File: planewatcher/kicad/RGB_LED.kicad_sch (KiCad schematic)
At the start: 4 parts

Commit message: Add persistent PCBWay BOM fields to KiCad schematic
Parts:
- D1: MPN (none) -> APHF1608SEEQBDZGKC; Manufacturer (none) -> Kingbright; Package (none) -> SOD-123F
- R3: MPN (none) -> RC0402FR-071KL; Manufacturer (none) -> Yageo; Package (none) -> 0402
- R4, R5: MPN (none) -> RC0402FR-07665RL; Manufacturer (none) -> Yageo; Package (none) -> 0402
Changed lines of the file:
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@@
+			)
+		)
+		(property "Package" "SOD-123F"
+			(at 111.76 83.82 0)
+			(hide yes)
+			(show_name no)
+			(do_not_autoplace no)
+			(effects
+				(font
+					(size 1.27 1.27)
+				)
+			)
+		)
+		(property "MPN" "APHF1608SEEQBDZGKC"
+			(at 111.76 83.82 0)
+			(hide yes)
+			(show_name no)
+			(do_not_autoplace no)
+			(effects
+				(font
+					(size 1.27 1.27)
+				)
+			)
+		)
+		(property "Manufacturer" "Kingbright"
+			(at 111.76 83.82 0)
+			(hide yes)
+			(show_name no)
+			(do_not_autoplace no)
+			(effects
+				(font
+					(size 1.27 1.27)
+				)
 			)
 		)
@@
 			)
 		)
+		(property "Package" "0402"
+			(at 133.35 87.63 0)
+			(hide yes)
+			(show_name no)
+			(do_not_autoplace no)
+			(effects
+				(font
+					(size 1.27 1.27)
+				)
+			)
+		)
+		(property "MPN" "RC0402FR-07665RL"
+			(at 133.35 87.63 0)
+			(hide yes)
+			(show_name no)
+			(do_not_autoplace no)
+			(effects
+				(font
+					(size 1.27 1.27)
+				)
+			)
+		)
+		(property "Manufacturer" "Yageo"
+			(at 133.35 87.63 0)
+			(hide yes)
+			(show_name no)
+			(do_not_autoplace no)
+			(effects
+				(font
+					(size 1.27 1.27)
+				)
+			)
+		)
 		(property "Suggested Part" "Yageo RC0402FR-07665RL"
 			(at 133.35 87.63 0)
@@
 			)
 		)
+		(property "Package" "0402"
+			(at 144.78 82.55 0)
+			(hide yes)
+			(show_name no)
+			(do_not_autoplace no)
+			(effects
+				(font
+					(size 1.27 1.27)
+				)
+			)
+		)
+		(property "MPN" "RC0402FR-07665RL"
+			(at 144.78 82.55 0)
+			(hide yes)
+			(show_name no)
+			(do_not_autoplace no)
+			(effects
+				(font
+					(size 1.27 1.27)
+				)
+			)
+		)
+		(property "Manufacturer" "Yageo"
+			(at 144.78 82.55 0)
+			(hide yes)
+			(show_name no)
+			(do_not_autoplace no)
+			(effects
+				(font
+					(size 1.27 1.27)
+				)
+			)
+		)
 		(property "Suggested Part" "Yageo RC0402FR-07665RL"
 			(at 144.78 82.55 0)
@@
 			(at 123.19 92.71 0)
 			(hide yes)
+			(show_name no)
+			(do_not_autoplace no)
+			(effects
+				(font
+					(size 1.27 1.27)
+				)
+			)
+		)
+		(property "Package" "0402"
+			(at 123.19 92.71 0)
+			(hide yes)
+			(show_name no)
+			(do_not_autoplace no)
+			(effects
+				(font
+					(size 1.27 1.27)
+				)
+			)
+		)
+		(property "MPN" "RC0402FR-071KL"
+			(at 123.19 92.71 0)
+			(hide yes)
+			(show_name no)
+			(do_not_autoplace no)
+			(effects
+				(font
+					(size 1.27 1.27)
+				)
+			)
+		)
+		(property "Manufacturer" "Yageo"
+			(at 123.19 92.71 0)
+			(hide yes)

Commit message: move power supply and add GPS module
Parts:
- renumbered D1 to LED4
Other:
- title: (none) -> Plane Watcher
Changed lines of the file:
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@@
 	(paper "A4")
 	(title_block
-		(date "2026-05-16")
-		(rev "prototype 1.1")
+		(title "Plane Watcher")
+		(date "2026-05-18")
+		(rev "prototype 1.2")
 		(company "plane.watch")
 	)
@@
 		(in_pos_files yes)
 		(dnp no)
-		(property "Reference" "D1"
+		(property "Reference" "LED4"
 			(at 111.76 71.12 0)
 			(show_name no)
@@
 			(project "planewatcher"
 				(path "/7a4a4324-e8b8-4d06-b75a-28095d4e9f10/52b32cc6-d826-42d3-aa96-9038a73a9bfc"
-					(reference "D5")
+					(reference "LED1")
 					(unit 1)
 				)
 				(path "/7a4a4324-e8b8-4d06-b75a-28095d4e9f10/59545c86-c058-4e69-82ad-a37ead5abf92"
-					(reference "D1")
+					(reference "LED4")
 					(unit 1)
 				)
 				(path "/7a4a4324-e8b8-4d06-b75a-28095d4e9f10/7739f02d-62c0-4bca-89eb-2791de83397a"
-					(reference "D4")
+					(reference "LED3")
 					(unit 1)
 				)
 				(path "/7a4a4324-e8b8-4d06-b75a-28095d4e9f10/8d837c64-f9ae-4d10-9c5f-d514a90db394"
-					(reference "D6")
+					(reference "LED5")
 					(unit 1)
 				)
 				(path "/7a4a4324-e8b8-4d06-b75a-28095d4e9f10/d4f7e37f-a721-4dfe-b190-52f36600c34c"
-					(reference "D7")
-					(unit 1)
-				)
+					(reference "LED2")
+					(unit 1)
+				)

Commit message: review & consolidate all capacitors
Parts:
- LED4: Suggested Part Kingbright APHF1608SEEQBDZGKC -> (none)
- R3: Suggested Part Yageo RC0402FR-071KL -> (none)
- R4, R5: Suggested Part Yageo RC0402FR-07665RL -> (none)
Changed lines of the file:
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@@
 			)
 		)
-		(property "Suggested Part" "Kingbright APHF1608SEEQBDZGKC"
+		(property "Purpose" "Common-anode RGB status indicator driven by FPGA GPIO pins."
 			(at 111.76 83.82 0)
 			(hide yes)
@@
 			)
 		)
-		(property "Purpose" "Common-anode RGB status indicator driven by FPGA GPIO pins."
+		(property "Mount_Type" ""
 			(at 111.76 83.82 0)
 			(hide yes)
@@
 			)
 		)
-		(property "Suggested Part" "Yageo RC0402FR-07665RL"
-			(at 133.35 87.63 0)
-			(hide yes)
-			(show_name no)
-			(do_not_autoplace no)
-			(effects
-				(font
-					(size 1.27 1.27)
-				)
-			)
-		)
 		(property "Purpose" "Current-limit resistor for an FPGA-driven RGB status LED channel."
+			(at 133.35 87.63 0)
+			(hide yes)
+			(show_name no)
+			(do_not_autoplace no)
+			(effects
+				(font
+					(size 1.27 1.27)
+				)
+			)
+		)
+		(property "Mount_Type" ""
 			(at 133.35 87.63 0)
 			(hide yes)
@@
 			)
 		)
-		(property "Suggested Part" "Yageo RC0402FR-07665RL"
-			(at 144.78 82.55 0)
-			(hide yes)
-			(show_name no)
-			(do_not_autoplace no)
-			(effects
-				(font
-					(size 1.27 1.27)
-				)
-			)
-		)
 		(property "Purpose" "Current-limit resistor for an FPGA-driven RGB status LED channel."
+			(at 144.78 82.55 0)
+			(hide yes)
+			(show_name no)
+			(do_not_autoplace no)
+			(effects
+				(font
+					(size 1.27 1.27)
+				)
+			)
+		)
+		(property "Mount_Type" ""
 			(at 144.78 82.55 0)
 			(hide yes)
@@
 			)
 		)
-		(property "Suggested Part" "Yageo RC0402FR-071KL"
-			(at 123.19 92.71 0)
-			(hide yes)
-			(show_name no)
-			(do_not_autoplace no)
-			(effects
-				(font
-					(size 1.27 1.27)
-				)
-			)
-		)
 		(property "Purpose" "Current-limit resistor for an FPGA-driven RGB status LED channel."
 			(at 123.19 92.71 0)
 			(hide yes)
+			(show_name no)
+			(do_not_autoplace no)
+			(effects
+				(font
+					(size 1.27 1.27)
+				)
+			)
+		)
+		(property "Mount_Type" ""
+			(at 123.19 92.71 0)
+			(hide yes)

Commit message: review & consolidate all resistors
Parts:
- R3, R4, R5: Manufacturer Yageo -> YAGEO; Package 0402 -> 0402 (1005 Metric)
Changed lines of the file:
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@@
 			)
 		)
-		(property "Datasheet" "https://www.yageogroup.com/component-documentation/download/specsheet/RC0402FR-07665RL"
-			(at 133.35 87.63 0)
-			(hide yes)
-			(show_name no)
-			(do_not_autoplace no)
-			(effects
-				(font
-					(size 1.27 1.27)
-				)
-			)
-		)
-		(property "Description" "665Ω, ±1%, thick film, 100ppm/°C, 0402 chip resistor"
-			(at 133.35 87.63 0)
-			(hide yes)
-			(show_name no)
-			(do_not_autoplace no)
-			(effects
-				(font
-					(size 1.27 1.27)
-				)
-			)
-		)
-		(property "Package" "0402"
+		(property "Datasheet" "https://yageogroup.com/content/datasheet/asset/file/PYU-RC_GROUP_51_ROHS_L"
+			(at 133.35 87.63 0)
+			(hide yes)
+			(show_name no)
+			(do_not_autoplace no)
+			(effects
+				(font
+					(size 1.27 1.27)
+				)
+			)
+		)
+		(property "Description" "665 Ohms ±1% 0.063W, 1/16W Chip Resistor 0402 (1005 Metric) Moisture Resistant Thick Film"
+			(at 133.35 87.63 0)
+			(hide yes)
+			(show_name no)
+			(do_not_autoplace no)
+			(effects
+				(font
+					(size 1.27 1.27)
+				)
+			)
+		)
+		(property "Package" "0402 (1005 Metric)"
 			(at 133.35 87.63 0)
 			(hide yes)
@@
 			)
 		)
-		(property "Manufacturer" "Yageo"
+		(property "Manufacturer" "YAGEO"
 			(at 133.35 87.63 0)
 			(hide yes)
@@
 			)
 		)
-		(property "Datasheet" "https://www.yageogroup.com/component-documentation/download/specsheet/RC0402FR-07665RL"
-			(at 144.78 82.55 0)
-			(hide yes)
-			(show_name no)
-			(do_not_autoplace no)
-			(effects
-				(font
-					(size 1.27 1.27)
-				)
-			)
-		)
-		(property "Description" "665Ω, ±1%, thick film, 100ppm/°C, 0402 chip resistor"
-			(at 144.78 82.55 0)
-			(hide yes)
-			(show_name no)
-			(do_not_autoplace no)
-			(effects
-				(font
-					(size 1.27 1.27)
-				)
-			)
-		)
-		(property "Package" "0402"
+		(property "Datasheet" "https://yageogroup.com/content/datasheet/asset/file/PYU-RC_GROUP_51_ROHS_L"
+			(at 144.78 82.55 0)
+			(hide yes)
+			(show_name no)
+			(do_not_autoplace no)
+			(effects
+				(font
+					(size 1.27 1.27)
+				)
+			)
+		)
+		(property "Description" "665 Ohms ±1% 0.063W, 1/16W Chip Resistor 0402 (1005 Metric) Moisture Resistant Thick Film"
+			(at 144.78 82.55 0)
+			(hide yes)
+			(show_name no)
+			(do_not_autoplace no)
+			(effects
+				(font
+					(size 1.27 1.27)
+				)
+			)
+		)
+		(property "Package" "0402 (1005 Metric)"
 			(at 144.78 82.55 0)
 			(hide yes)
@@
 			)
 		)
-		(property "Manufacturer" "Yageo"
+		(property "Manufacturer" "YAGEO"
 			(at 144.78 82.55 0)
 			(hide yes)
@@
 			)
 		)
-		(property "Datasheet" "https://www.yageogroup.com/component-documentation/download/specsheet/RC0402FR-071KL"
-			(at 123.19 92.71 0)
-			(hide yes)
-			(show_name no)
-			(do_not_autoplace no)
-			(effects
-				(font
-					(size 1.27 1.27)
-				)
-			)
-		)
-		(property "Description" "1kΩ, ±1%, thick film, 100ppm/°C, 0402 chip resistor"
-			(at 123.19 92.71 0)
-			(hide yes)
-			(show_name no)
-			(do_not_autoplace no)
-			(effects
-				(font
-					(size 1.27 1.27)
-				)
-			)
-		)
-		(property "Package" "0402"
+		(property "Datasheet" "https://yageogroup.com/content/datasheet/asset/file/PYU-RC_GROUP_51_ROHS_L"
+			(at 123.19 92.71 0)
+			(hide yes)
+			(show_name no)
+			(do_not_autoplace no)
+			(effects
+				(font
+					(size 1.27 1.27)
+				)
+			)
+		)
+		(property "Description" "1 kOhms ±1% 0.063W, 1/16W Chip Resistor 0402 (1005 Metric) Moisture Resistant Thick Film"
+			(at 123.19 92.71 0)
+			(hide yes)
+			(show_name no)
+			(do_not_autoplace no)
+			(effects
+				(font
+					(size 1.27 1.27)
+				)
+			)
+		)
+		(property "Package" "0402 (1005 Metric)"
 			(at 123.19 92.71 0)
 			(hide yes)
@@
 			)
 		)
-		(property "Manufacturer" "Yageo"
-			(at 123.19 92.71 0)
-			(hide yes)
+		(property "Manufacturer" "YAGEO"
+			(at 123.19 92.71 0)
+			(hide yes)

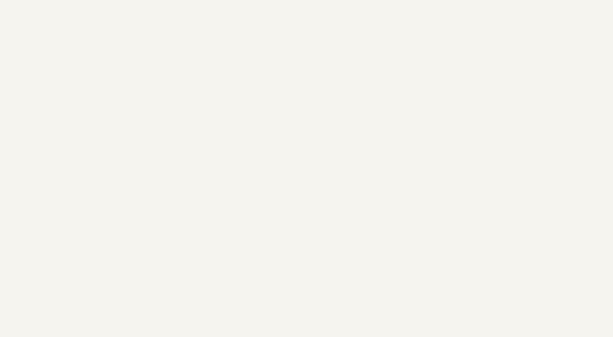
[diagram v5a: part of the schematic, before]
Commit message: add license & copyright info to schematic and pcb. fix layer window.
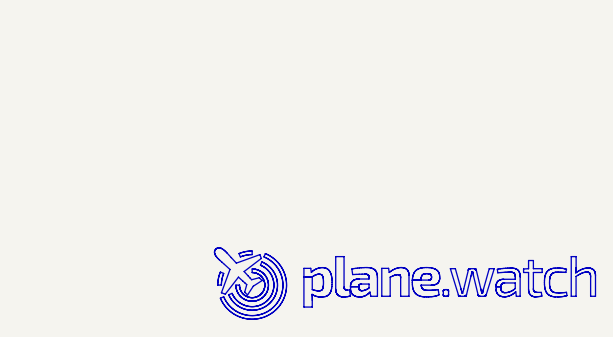
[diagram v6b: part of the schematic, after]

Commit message: added lcsc_ids to all parts
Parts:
- LED4: lcsc_id (none) -> C5145179
- R3: lcsc_id (none) -> C2935237
- R4, R5: lcsc_id (none) -> C477780
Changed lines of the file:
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@@
+			)
+		)
+		(property "lcsc_id" "C5145179"
+			(at 111.76 83.82 0)
+			(hide yes)
+			(show_name no)
+			(do_not_autoplace no)
+			(effects
+				(font
+					(size 1.27 1.27)
+				)
 			)
 		)
@@
 			)
 		)
+		(property "lcsc_id" "C477780"
+			(at 133.35 87.63 0)
+			(hide yes)
+			(show_name no)
+			(do_not_autoplace no)
+			(effects
+				(font
+					(size 1.27 1.27)
+				)
+			)
+		)
 		(pin "2"
 		)
@@
 			)
 		)
+		(property "lcsc_id" "C477780"
+			(at 144.78 82.55 0)
+			(hide yes)
+			(show_name no)
+			(do_not_autoplace no)
+			(effects
+				(font
+					(size 1.27 1.27)
+				)
+			)
+		)
 		(pin "2"
 		)
@@
 			(at 123.19 92.71 0)
 			(hide yes)
+			(show_name no)
+			(do_not_autoplace no)
+			(effects
+				(font
+					(size 1.27 1.27)
+				)
+			)
+		)
+		(property "lcsc_id" "C2935237"
+			(at 123.19 92.71 0)
+			(hide yes)

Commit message: change discontinued parts
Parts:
- R3: lcsc_id C2935237 -> C106235
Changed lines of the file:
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@@
 			)
 		)
-		(property "lcsc_id" "C2935237"
+		(property "lcsc_id" "C106235"
 			(at 123.19 92.71 0)
 			(hide yes)
